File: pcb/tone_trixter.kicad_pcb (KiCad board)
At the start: 2 copper layers, 132 x 57 mm, 0 parts

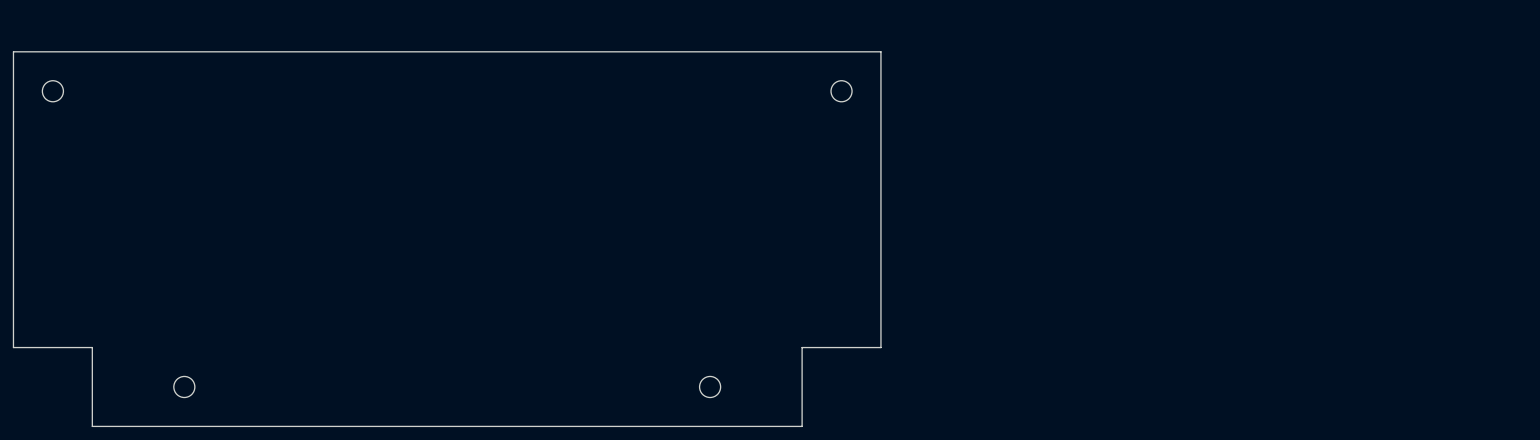
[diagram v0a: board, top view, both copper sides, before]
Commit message: pcb: board checkpoint -- placement so far + 10x10 notch outline, no holes
Captures the first-pass placement (anchors + hand-rotations) and the
updated Edge.Cuts outline (10x10 corner notches, mounting holes removed).

Co-Authored-By: Claude Opus 4.8 <noreply@anthropic.com>
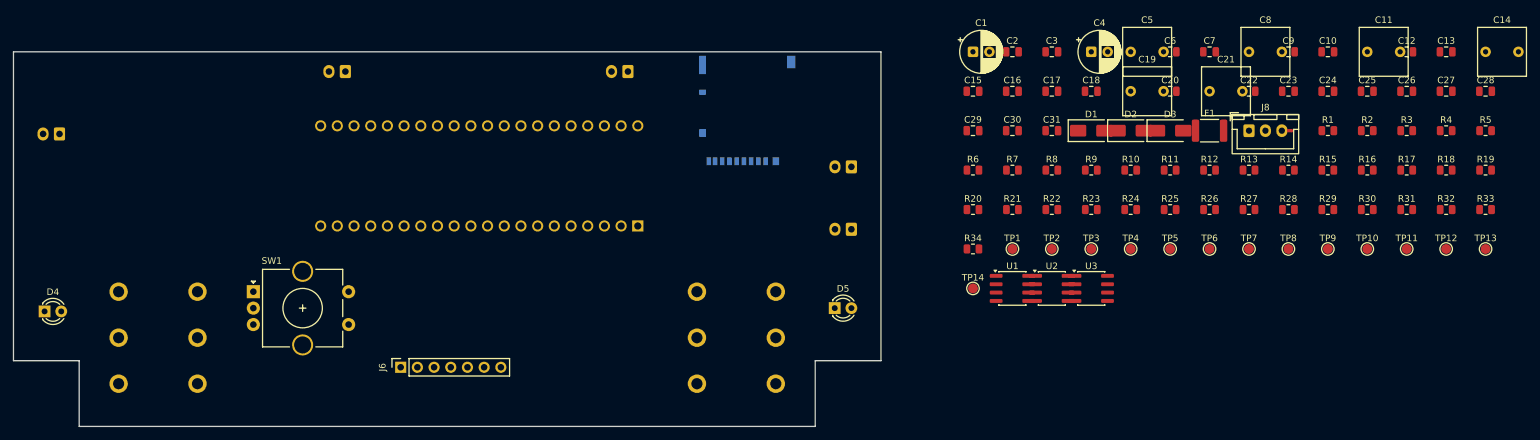
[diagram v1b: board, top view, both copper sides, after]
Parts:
- added C1: 100u/25V, Capacitor_THT:CP_Radial_D6.3mm_P2.50mm, F.Cu at (176.0, 30.0)
- added C10: 33n, Capacitor_SMD:C_0805_2012Metric, F.Cu at (230.0, 30.0)
- added C11: 10u film, Capacitor_THT:C_Rect_L7.2mm_W7.2mm_P5.00mm_FKS2_FKP2_MKS2_MKP2, F.Cu at (236.0, 30.0)
- added C12: 100p, Capacitor_SMD:C_0805_2012Metric, F.Cu at (242.0, 30.0)
- added C13: 1n, Capacitor_SMD:C_0805_2012Metric, F.Cu at (248.0, 30.0)
- added C14: 10u film, Capacitor_THT:C_Rect_L7.2mm_W7.2mm_P5.00mm_FKS2_FKP2_MKS2_MKP2, F.Cu at (254.0, 30.0)
- added C15: 330p, Capacitor_SMD:C_0805_2012Metric, F.Cu at (176.0, 36.0)
- added C16: 33n, Capacitor_SMD:C_0805_2012Metric, F.Cu at (182.0, 36.0)
- added C17: 100n, Capacitor_SMD:C_0805_2012Metric, F.Cu at (188.0, 36.0)
- added C18: 10u, Capacitor_SMD:C_0805_2012Metric, F.Cu at (194.0, 36.0)
- added C19: 10u film, Capacitor_THT:C_Rect_L7.2mm_W7.2mm_P5.00mm_FKS2_FKP2_MKS2_MKP2, F.Cu at (200.0, 36.0)
- added C2: 10u, Capacitor_SMD:C_0805_2012Metric, F.Cu at (182.0, 30.0)
- added C20: 100p, Capacitor_SMD:C_0805_2012Metric, F.Cu at (206.0, 36.0)
- added C21: 10u film, Capacitor_THT:C_Rect_L7.2mm_W7.2mm_P5.00mm_FKS2_FKP2_MKS2_MKP2, F.Cu at (212.0, 36.0)
- added C22: 100n, Capacitor_SMD:C_0805_2012Metric, F.Cu at (218.0, 36.0)
- added C23: 100n, Capacitor_SMD:C_0805_2012Metric, F.Cu at (224.0, 36.0)
- added C24: 100n, Capacitor_SMD:C_0805_2012Metric, F.Cu at (230.0, 36.0)
- added C25: 100n, Capacitor_SMD:C_0805_2012Metric, F.Cu at (236.0, 36.0)
- added C26: 10n, Capacitor_SMD:C_0805_2012Metric, F.Cu at (242.0, 36.0)
- added C27: 10n, Capacitor_SMD:C_0805_2012Metric, F.Cu at (248.0, 36.0)
- added C28: 10n, Capacitor_SMD:C_0805_2012Metric, F.Cu at (254.0, 36.0)
- added C29: 100n, Capacitor_SMD:C_0805_2012Metric, F.Cu at (176.0, 42.0)
- added C3: 100n, Capacitor_SMD:C_0805_2012Metric, F.Cu at (188.0, 30.0)
- added C30: 100n, Capacitor_SMD:C_0805_2012Metric, F.Cu at (182.0, 42.0)
- added C31: 100n, Capacitor_SMD:C_0805_2012Metric, F.Cu at (188.0, 42.0)
- added C4: 100u/25V, Capacitor_THT:CP_Radial_D6.3mm_P2.50mm, F.Cu at (194.0, 30.0)
- added C5: 10u film, Capacitor_THT:C_Rect_L7.2mm_W7.2mm_P5.00mm_FKS2_FKP2_MKS2_MKP2, F.Cu at (200.0, 30.0)
- added C6: 100p, Capacitor_SMD:C_0805_2012Metric, F.Cu at (206.0, 30.0)
- added C7: 1n, Capacitor_SMD:C_0805_2012Metric, F.Cu at (212.0, 30.0)
- added C8: 10u film, Capacitor_THT:C_Rect_L7.2mm_W7.2mm_P5.00mm_FKS2_FKP2_MKS2_MKP2, F.Cu at (218.0, 30.0)
- added C9: 330p, Capacitor_SMD:C_0805_2012Metric, F.Cu at (224.0, 30.0)
- added D1: SS34, Diode_SMD:D_SMA, F.Cu at (194.0, 42.0)
- added D2: SS34, Diode_SMD:D_SMA, F.Cu at (200.0, 42.0)
- added D3: SMAJ15A, Diode_SMD:D_SMA, F.Cu at (206.0, 42.0)
- added D4: 3mm engaged, LED_THT:LED_D3.0mm, F.Cu at (34.7, 69.5)
- added D5: 3mm record, LED_THT:LED_D3.0mm, F.Cu at (155.0, 69.0)
- added F1: 500mA, Fuse:Fuse_1812_4532Metric, F.Cu at (212.0, 42.0)
- added J1: INA jack lead, TT:K3599_TRS_6leg, B.Cu at (52.0, 73.5)
- added J10: microSD DM3AT, Connector_Card:microSD_HC_Hirose_DM3AT-SF-PEJM5, B.Cu at (141.7, 38.9)
- added J2: OUT jack lead, TT:K3599_TRS_6leg, B.Cu at (140.0, 73.5)
- added J3: DC 2.1mm lead, Connector_JST:JST_XH_B2B-XH-A_1x02_P2.50mm_Vertical, B.Cu at (157.5, 57.0)
- added J4: Battery lead, Connector_JST:JST_XH_B2B-XH-A_1x02_P2.50mm_Vertical, B.Cu at (157.5, 47.5)
- added J5: Enclosure bond, Connector_JST:JST_XH_B2B-XH-A_1x02_P2.50mm_Vertical, B.Cu at (37.0, 42.5)
- added J6: OLED 1.3" 7-pin, Connector_PinSocket_2.54mm:PinSocket_1x07_P2.54mm_Vertical, F.Cu at (88.9, 78.0)
- added J7: SW-L bypass, Connector_JST:JST_XH_B2B-XH-A_1x02_P2.50mm_Vertical, B.Cu at (80.5, 33.0)
- added J8: INB jack lead, Connector_JST:JST_XH_B3B-XH-A_1x03_P2.50mm_Vertical, F.Cu at (218.0, 42.0)
- added J9: SW-R tuner, Connector_JST:JST_XH_B2B-XH-A_1x02_P2.50mm_Vertical, B.Cu at (123.5, 33.0)
- added NT1: STAR, NetTie:NetTie-2_SMD_Pad0.5mm, F.Cu at (224.0, 42.0)
- added R1: 100R, Resistor_SMD:R_0805_2012Metric, F.Cu at (230.0, 42.0)
- added R10: 100R, Resistor_SMD:R_0805_2012Metric, F.Cu at (200.0, 48.0)
- added R11: 3k3, Resistor_SMD:R_0805_2012Metric, F.Cu at (206.0, 48.0)
- added R12: 4k7 (DNP=no pad), Resistor_SMD:R_0805_2012Metric, F.Cu at (212.0, 48.0)
- added R13: 10k, Resistor_SMD:R_0805_2012Metric, F.Cu at (218.0, 48.0)
- added R14: 10k, Resistor_SMD:R_0805_2012Metric, F.Cu at (224.0, 48.0)
- added R15: 100R, Resistor_SMD:R_0805_2012Metric, F.Cu at (230.0, 48.0)
- added R16: 1M, Resistor_SMD:R_0805_2012Metric, F.Cu at (236.0, 48.0)
- added R17: 470k, Resistor_SMD:R_0805_2012Metric, F.Cu at (242.0, 48.0)
- added R18: 15k, Resistor_SMD:R_0805_2012Metric, F.Cu at (248.0, 48.0)
- added R19: 15k, Resistor_SMD:R_0805_2012Metric, F.Cu at (254.0, 48.0)
- added R2: 1M, Resistor_SMD:R_0805_2012Metric, F.Cu at (236.0, 42.0)
- added R20: 0R (18k = +7 dB), Resistor_SMD:R_0805_2012Metric, F.Cu at (176.0, 54.0)
- added R21: 100R, Resistor_SMD:R_0805_2012Metric, F.Cu at (182.0, 54.0)
- added R22: 10k, Resistor_SMD:R_0805_2012Metric, F.Cu at (188.0, 54.0)
- added R23: 33R, Resistor_SMD:R_0805_2012Metric, F.Cu at (194.0, 54.0)
- added R24: 33R, Resistor_SMD:R_0805_2012Metric, F.Cu at (200.0, 54.0)
- added R25: 4k7, Resistor_SMD:R_0805_2012Metric, F.Cu at (206.0, 54.0)
- added R26: 4k7, Resistor_SMD:R_0805_2012Metric, F.Cu at (212.0, 54.0)
- added R27: 10k, Resistor_SMD:R_0805_2012Metric, F.Cu at (218.0, 54.0)
- added R28: 10k, Resistor_SMD:R_0805_2012Metric, F.Cu at (224.0, 54.0)
- added R29: 10k, Resistor_SMD:R_0805_2012Metric, F.Cu at (230.0, 54.0)
- added R3: 100R, Resistor_SMD:R_0805_2012Metric, F.Cu at (242.0, 42.0)
- added R30: 10k, Resistor_SMD:R_0805_2012Metric, F.Cu at (236.0, 54.0)
- added R31: 10k, Resistor_SMD:R_0805_2012Metric, F.Cu at (242.0, 54.0)
- added R32: 1k, Resistor_SMD:R_0805_2012Metric, F.Cu at (248.0, 54.0)
- added R33: 1k, Resistor_SMD:R_0805_2012Metric, F.Cu at (254.0, 54.0)
- added R34: 10k, Resistor_SMD:R_0805_2012Metric, F.Cu at (176.0, 60.0)
- added R4: 3k3, Resistor_SMD:R_0805_2012Metric, F.Cu at (248.0, 42.0)
- added R5: 4k7 (DNP=no pad), Resistor_SMD:R_0805_2012Metric, F.Cu at (254.0, 42.0)
- added R6: 10k, Resistor_SMD:R_0805_2012Metric, F.Cu at (176.0, 48.0)
- added R7: 10k, Resistor_SMD:R_0805_2012Metric, F.Cu at (182.0, 48.0)
- added R8: 100R, Resistor_SMD:R_0805_2012Metric, F.Cu at (188.0, 48.0)
- added R9: 1M, Resistor_SMD:R_0805_2012Metric, F.Cu at (194.0, 48.0)
- added SW1: PEC11R-4220F-S0024, Rotary_Encoder:RotaryEncoder_Alps_EC11E-Switch_Vertical_H20mm_CircularMountingHoles, F.Cu at (66.5, 66.5)
- added TP1: IN1_TIP, TestPoint:TestPoint_Pad_D1.5mm, F.Cu at (182.0, 60.0)
- added TP10: +9VA, TestPoint:TestPoint_Pad_D1.5mm, F.Cu at (236.0, 60.0)
- added TP11: +3V3D, TestPoint:TestPoint_Pad_D1.5mm, F.Cu at (242.0, 60.0)
- added TP12: +3V3A, TestPoint:TestPoint_Pad_D1.5mm, F.Cu at (248.0, 60.0)
- added TP13: GNDA, TestPoint:TestPoint_Pad_D1.5mm, F.Cu at (254.0, 60.0)
- added TP14: GNDD, TestPoint:TestPoint_Pad_D1.5mm, F.Cu at (176.0, 66.0)
- added TP2: AA_OUT, TestPoint:TestPoint_Pad_D1.5mm, F.Cu at (188.0, 60.0)
- added TP3: AIN1, TestPoint:TestPoint_Pad_D1.5mm, F.Cu at (194.0, 60.0)
- added TP4: IN2_TIP, TestPoint:TestPoint_Pad_D1.5mm, F.Cu at (200.0, 60.0)
- added TP5: AB_OUT, TestPoint:TestPoint_Pad_D1.5mm, F.Cu at (206.0, 60.0)
- added TP6: AIN2, TestPoint:TestPoint_Pad_D1.5mm, F.Cu at (212.0, 60.0)
- added TP7: VREF, TestPoint:TestPoint_Pad_D1.5mm, F.Cu at (218.0, 60.0)
- added TP8: OUT_TIP, TestPoint:TestPoint_Pad_D1.5mm, F.Cu at (224.0, 60.0)
- added TP9: VIN, TestPoint:TestPoint_Pad_D1.5mm, F.Cu at (230.0, 60.0)
- added U1: OPA1642AIDR, Package_SO:SOIC-8_3.9x4.9mm_P1.27mm, F.Cu at (182.0, 66.0)
- added U2: OPA1642AIDR, Package_SO:SOIC-8_3.9x4.9mm_P1.27mm, F.Cu at (188.0, 66.0)
- added U3: OPA1642AIDR, Package_SO:SOIC-8_3.9x4.9mm_P1.27mm, F.Cu at (194.0, 66.0)
- added U4: Daisy Seed3, Module:Electrosmith_Daisy_Seed, B.Cu at (125.0, 56.5)
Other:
- outline, holes or cut-outs redrawn

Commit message: pcb: cluster passives by function; preserve builder's anchor placement
gen_place.py now captures the builder's hand-placed enclosure anchors
(2026-10-10 layout: Seed right, encoder left, jacks on the back, etc.)
and only places the 3 OPAs + Ch-B and clusters the 84 passives by
connectivity into the open centre: front-end A around U1, front-end B
around U2, output around U3, Seed decoupling + SD around U4, power
section, and a misc group (film caps/star/TPs) to sort by hand. Groups
are compact blocks to drag to final homes. 101 footprints intact.

Co-Authored-By: Claude Opus 4.8 <noreply@anthropic.com>
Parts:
- moved R33 178.2 mm to (78.0, 81.6)
- moved R19 176.5 mm to (78.0, 61.4)
- moved C28 176.2 mm to (81.4, 71.4)
- moved C27 173.6 mm to (78.0, 71.4)
- moved R5 172.6 mm to (81.4, 41.4)
- moved R4 170.0 mm to (78.0, 41.4)
- moved C12 165.0 mm to (78.0, 48.0)
- moved R32 158.3 mm to (91.6, 78.2)
- moved TP12 157.1 mm to (91.6, 44.8)
- moved R18 156.7 mm to (91.6, 58.0)
- moved C10 156.7 mm to (78.0, 68.0)
- moved R31 155.7 mm to (88.2, 78.2)
- moved R17 154.1 mm to (88.2, 58.0)
- moved C26 153.8 mm to (91.6, 68.0)
- moved R30 153.1 mm to (84.8, 78.2)
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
